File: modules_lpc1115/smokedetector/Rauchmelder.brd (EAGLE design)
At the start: 38 x 65 mm, 75 parts, among them IC100 BD9G101, IC2 LPC1115, Q1 BC856, Q3 BCP52, Q4 ASFL, T1 BC847C, T2 BC817

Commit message: [RM] - power feedback protection added
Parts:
- added D11: BAT54SDW-7-F, MyDiode:SOT363
- added D12: BAT54WS-7-F, MyDiode:SOD323
- added R20: 0R, MyRCL:R0805
- moved FD3 18.0 mm to (36.9, 50.9)
- moved D2 0.80 mm to (26.6, 43.8)
- moved D6 0.80 mm to (24.5, 43.9)
- moved Q1 0.40 mm to (20.7, 44.7)
- moved R16 0.40 mm to (21.2, 41.4)
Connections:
- net GND: now also D11.1, D11.4, R20.1
- net LT5: now also R20.2
- net N$1: now also D11.2, D11.5, D12.A
- net N$18: now also D12.C
- net RXD: now also D11.6
- net TXD: now also D11.3
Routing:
- net RXD: track 43.8 -> 68.8 mm
- net TXD: track 44.7 -> 65.4 mm
- net N$1: track 9.86 -> 25.7 mm
- net LT5: track 41.8 -> 51.4 mm, vias 1 -> 2
- net GND: track 48.3 -> 52.9 mm, vias 83 -> 76
- net +3V3: track 160.9 -> 158.2 mm
- net N$18: track 8.47 -> 9.32 mm, vias 0 -> 1

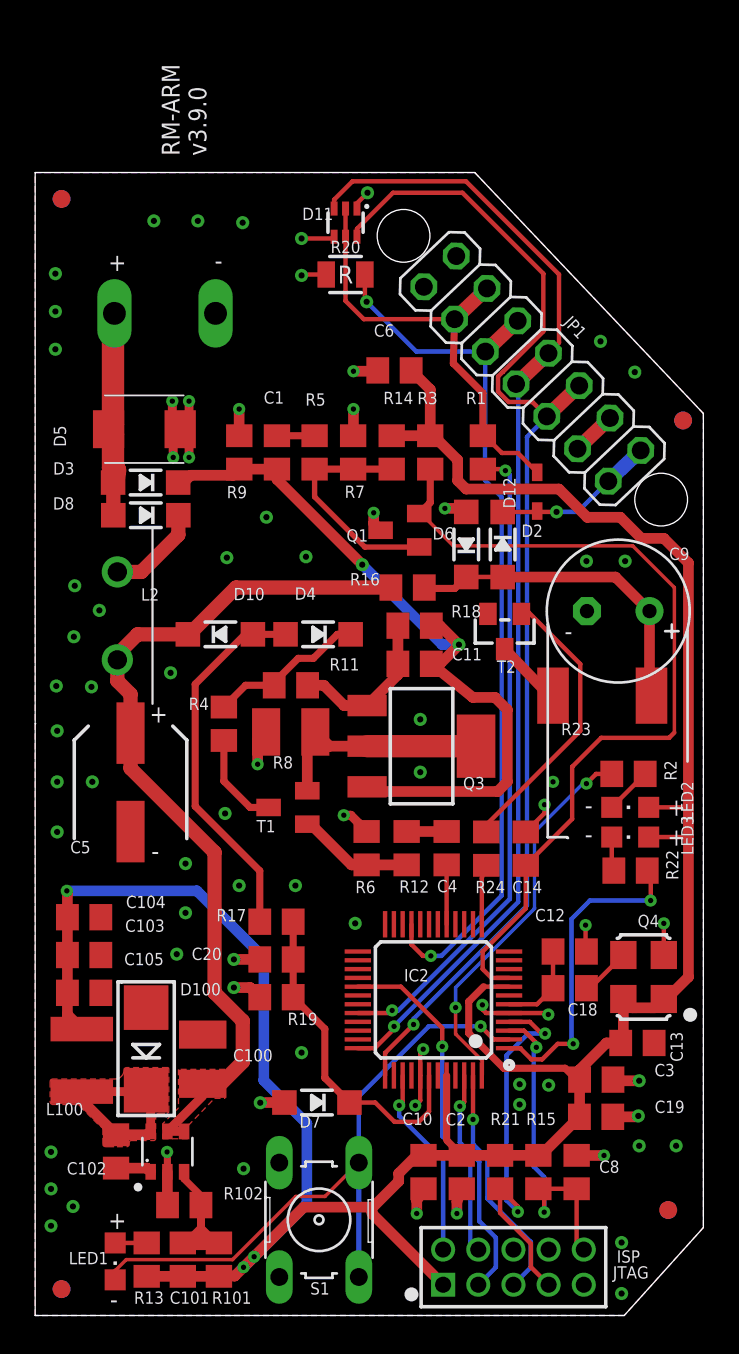
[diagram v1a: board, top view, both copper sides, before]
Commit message: [RM] - updated silk screen
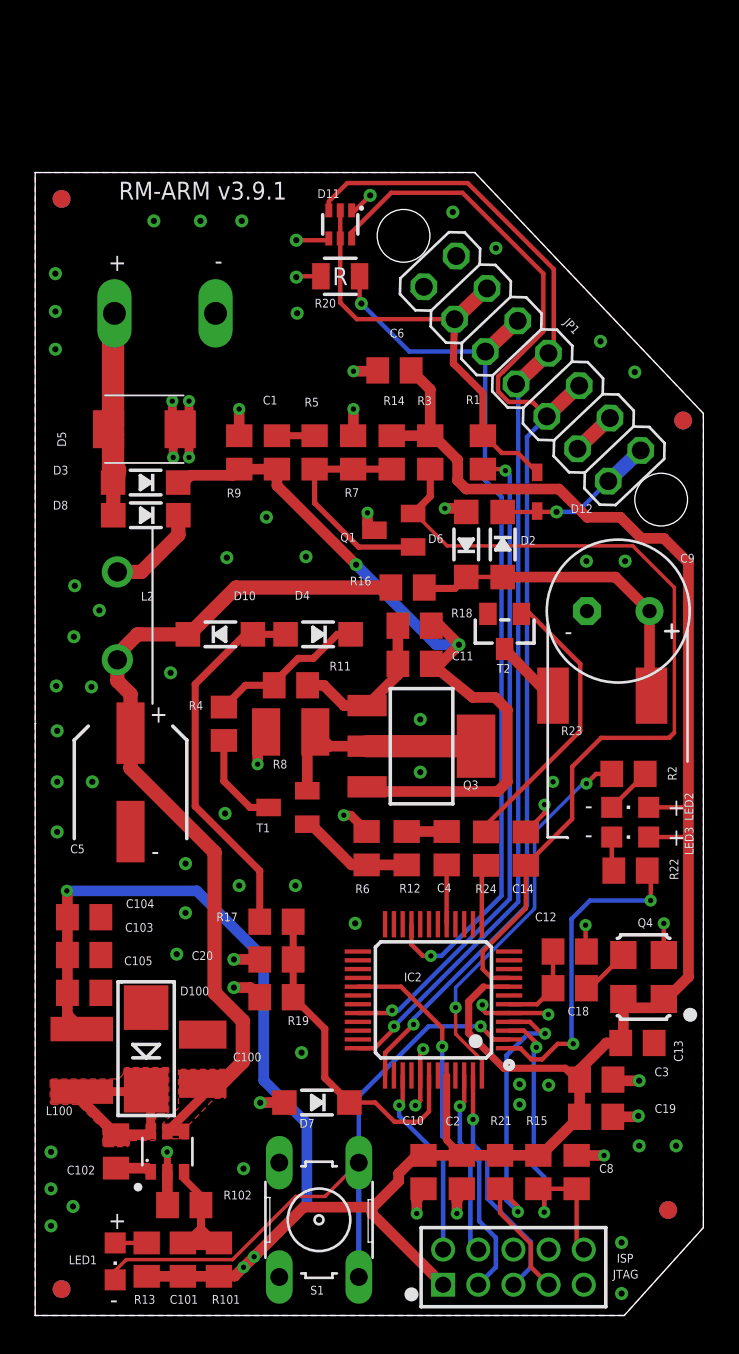
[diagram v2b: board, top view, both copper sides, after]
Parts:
- moved Q1 0.35 mm to (20.4, 44.7)
- moved D11 0.32 mm to (17.4, 62.0)
- moved R20 0.32 mm to (17.4, 59.1)
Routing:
- net GND: track 52.9 -> 53.2 mm, vias 76 -> 79
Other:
- board text added: "RM-ARM v3.9.1"
- board text removed: "RM-ARM v3.9.0"

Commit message: [RM] - changed D100 to SOD-123 again, added iBom, added .sch PDF
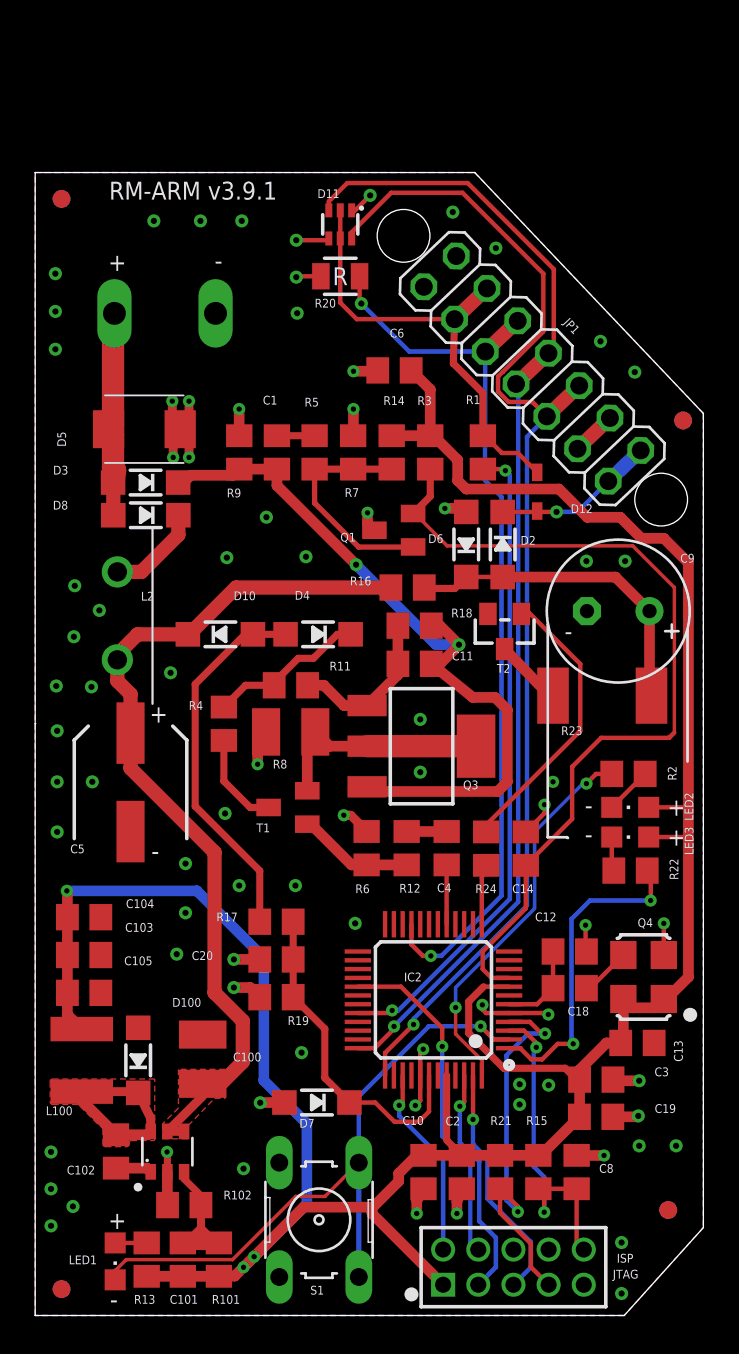
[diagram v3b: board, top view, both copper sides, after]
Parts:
- D100: device SamacSys_Parts:SMADIODE -> SamacSys_Parts:SOD-123
- moved D100 0.79 mm to (5.86, 14.5)
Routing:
- net LX: track 11.6 -> 10.9 mm
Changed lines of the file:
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@@
 <text x="6.6012" y="25.920575" size="1.016" layer="21" ratio="10">-</text>
 <text x="30.1012" y="38.420575" size="1.016" layer="21" ratio="10">-</text>
-<text x="4.754375" y="63.4619" size="1.016" layer="21" ratio="7">RM-ARM v3.9.1</text>
+<text x="4.204375" y="63.4619" size="1.016" layer="21" ratio="7">RM-ARM v3.9.1</text>
 <wire x1="29.15" y1="39.3" x2="29.15" y2="27.2" width="0.1524" layer="21"/>
 <wire x1="29.15" y1="27.2" x2="30.25" y2="27.2" width="0.1524" layer="21"/>
@@
 <attribute name="VALUE" x="7.4525875" y="0.156" size="0.5" layer="27"/>
 </element>
-<element name="D100" library="SamacSys_Parts" library_urn="urn:adsk.eagle:library:40006276" package="SMADIODE" package3d_urn="urn:adsk.eagle:package:41867658/1" value="RB060M-60" x="6.31" y="15.1613" smashed="yes" rot="R90">
-<attribute name="NAME" x="8.2413" y="18.206" size="0.5" layer="25" ratio="18"/>
-<attribute name="VALUE" x="8.2413" y="17.562" size="0.5" layer="27" ratio="10"/>
+<element name="D100" library="SamacSys_Parts" library_urn="urn:adsk.eagle:library:40006276" package="SOD-123" package3d_urn="urn:adsk.eagle:package:40015434/2" value="RB060M-60" x="5.86" y="14.5113" smashed="yes" rot="R90">
+<attribute name="NAME" x="7.7913" y="17.556" size="0.5" layer="25" ratio="18"/>
+<attribute name="VALUE" x="7.7913" y="16.912" size="0.5" layer="27" ratio="10"/>
 </element>
 <element name="FD1" library="Fiducial" package="FID_040" value="FID_40MIL" x="1.5" y="63.5" smashed="yes">
@@
 <contactref element="L100" pad="1"/>
 <contactref element="D100" pad="C"/>
-<wire x1="6.569" y1="10.47" x2="6.569" y2="12.78423125" width="0.508" layer="1"/>
-<wire x1="6.569" y1="12.78423125" x2="6.31" y2="12.8118" width="0.508" layer="1"/>
-<wire x1="6.31" y1="12.8118" x2="6.300109375" y2="12.7333" width="0.508" layer="1"/>
-<wire x1="6.300109375" y1="12.7333" x2="2.65" y2="12.7333" width="0.508" layer="1"/>
+<wire x1="6.569" y1="10.47" x2="6.569" y2="11.218475" width="0.508" layer="1"/>
+<wire x1="6.569" y1="11.218475" x2="5.86" y2="12.6613" width="0.508" layer="1"/>
+<wire x1="5.86" y1="12.6613" x2="5.85876875" y2="12.7333" width="0.508" layer="1"/>
+<wire x1="5.85876875" y1="12.7333" x2="2.65" y2="12.7333" width="0.508" layer="1"/>
 <wire x1="4.599" y1="10.28" x2="2.65" y2="12.229" width="0.6096" layer="1"/>
 <wire x1="2.65" y1="12.229" x2="2.65" y2="12.7333" width="0.6096" layer="1"/>
@@
 <wire x1="6.379" y1="10.28" x2="6.569" y2="10.47" width="0.6096" layer="1"/>
 <polygon width="0.0762" layer="1" thermals="no">
-<vertex x="4.65" y="9.6"/>
+<vertex x="4" y="9.6"/>
 <vertex x="5.2" y="9.6" curve="90"/>
 <vertex x="5.35" y="9.75"/>
@@
 <vertex x="5.45" y="9.95"/>
 <vertex x="6.75" y="9.95" curve="90"/>
-<vertex x="6.85" y="10.05"/>
-<vertex x="6.85" y="11.3" curve="-90"/>
-<vertex x="7.05" y="11.5"/>
-<vertex x="7.5" y="11.5" curve="90"/>
-<vertex x="7.6" y="11.6"/>
-<vertex x="7.6" y="14.05" curve="90"/>
-<vertex x="7.55" y="14.1"/>
-<vertex x="5.2" y="14.1" curve="90"/>
-<vertex x="5.05" y="13.95" curve="-90"/>
-<vertex x="4.55" y="13.45"/>
+<vertex x="6.8" y="10"/>
+<vertex x="6.8" y="13.45"/>
 <vertex x="1" y="13.45" curve="90"/>
 <vertex x="0.85" y="13.3"/>
@@
 <vertex x="3.7" y="10.75" curve="-90"/>
 <vertex x="3.85" y="10.6"/>
-<vertex x="3.85" y="10.1"/>
 <vertex x="3.85" y="9.75" curve="90"/>
-<vertex x="4" y="9.6"/>
-<vertex x="4.15" y="9.6"/>
 </polygon>
 </signal>
